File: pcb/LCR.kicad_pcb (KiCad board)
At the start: 2 copper layers, 63.5 x 25.9 mm, 97 parts, among them J1 Conn_01x02_Pin, J2 USB_C_Receptacle, J3 Conn_01x04_Socket, J4 Conn_01x01_Pin, J5 Conn_01x01_Pin, Q1 BSP613, SW1 SW_SPDT, SW2 SW_DIP_x02, SW3 SW_SPST, U1 LM1117DT-3.3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

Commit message: Add/fix missing/wrong vendor(id)
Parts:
- F2: value 150m -> 350m
- F3: value 10mA -> 10m
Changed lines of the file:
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@@
     (property "Sheetfile" "LCR_measurement.kicad_sch")
     (property "Sheetname" "Measurement")
+    (property "Vendor" "DigiKey")
+    (property "VendorId" "MCP6001T-I/OTCT-ND")
     (property "ki_description" "1MHz, Low-Power Op Amp, SOT-23-5")
     (property "ki_keywords" "single opamp")
@@
     (property "Sheetname" "Measurement")
     (property "Vendor" "HTL")
-    (property "VendorId" "100128")
+    (property "VendorId" "103341")
     (property "ki_description" "Unpolarized capacitor")
     (property "ki_keywords" "cap capacitor")
@@
     (property "Sheetfile" "LCR_measurement.kicad_sch")
     (property "Sheetname" "Measurement")
+    (property "Vendor" "HTL")
+    (property "VendorId" "100206")
     (property "ki_description" "Schottky diode")
     (property "ki_keywords" "diode Schottky")
@@
     (property "Sheetfile" "LCR.kicad_sch")
     (property "Sheetname" "")
+    (property "Vendor" "HTL")
+    (property "VendorId" "103444")
     (property "ki_description" "800mA Low-Dropout Linear Regulator, 3.3V fixed output, TO-252")
     (property "ki_keywords" "linear regulator ldo fixed positive")
@@
     (property "Sheetfile" "LCR_measurement.kicad_sch")
     (property "Sheetname" "Measurement")
+    (property "Vendor" "DigiKey")
+    (property "VendorId" "150-MCP3562RT-E/STCT-ND")
     (property "ki_keywords" "MCP3562RT-E/ST")
     (attr smd)
@@
     (property "Sheetfile" "LCR_measurement.kicad_sch")
     (property "Sheetname" "Measurement")
-    (property "Vendor" "HTL")
-    (property "VendorId" "101546")
+    (property "Vendor" "Amazon")
+    (property "VendorId" "B07BDFXFRK")
     (property "ki_description" "Generic connector, single row, 01x04, script generated")
     (property "ki_keywords" "connector")
@@
     (property "Sheetfile" "LCR_measurement.kicad_sch")
     (property "Sheetname" "Measurement")
+    (property "Vendor" "HTL")
+    (property "VendorId" "100206")
     (property "ki_description" "Schottky diode")
     (property "ki_keywords" "diode Schottky")
@@
     (property "Sheetname" "")
     (property "Vendor" "HTL")
-    (property "VendorId" "")
+    (property "VendorId" "101639")
     (property "ki_description" "Fuse")
     (property "ki_keywords" "fuse")
@@
         (effects (font (size 0.6 0.6) (thickness 0.12)))
     )
-    (fp_text value "150m" (at 0 1.82) (layer "F.Fab")
+    (fp_text value "350m" (at 0 1.82) (layer "F.Fab")
         (effects (font (size 1 1) (thickness 0.15)))
     )
@@
     (property "Sheetfile" "LCR_measurement.kicad_sch")
     (property "Sheetname" "Measurement")
+    (property "Vendor" "DigiKey")
+    (property "VendorId" "MCP4921T-E/MSCT-ND")
     (property "ki_description" "12-Bit D/A Converters with SPI Interface")
     (property "ki_keywords" "12-Bit DAC SPI 1ch")
@@
     (property "Sheetname" "Measurement")
     (property "Vendor" "HTL")
-    (property "VendorId" "102944")
+    (property "VendorId" "102967")
     (property "ki_description" "Resistor")
     (property "ki_keywords" "R res resistor")
@@
     (property "Sheetfile" "LCR.kicad_sch")
     (property "Sheetname" "")
-    (property "Vendor" "HTL")
-    (property "VendorId" "101017, 101382")
+    (property "Vendor" "")
+    (property "VendorId" "")
     (property "ki_description" "Mounting Hole with connection")
     (property "ki_keywords" "mounting hole")
@@
     (property "Sheetname" "Measurement")
     (property "Vendor" "HTL")
-    (property "VendorId" "102944")
+    (property "VendorId" "102967")
     (property "ki_description" "Resistor")
     (property "ki_keywords" "R res resistor")
@@
     (property "Sheetfile" "LCR_measurement.kicad_sch")
     (property "Sheetname" "Measurement")
+    (property "Vendor" "HTL")
+    (property "VendorId" "101614")
     (property "ki_description" "Single Pole Single Throw (SPST) switch")
     (property "ki_keywords" "switch lever")
@@
     (property "Sheetfile" "LCR_measurement.kicad_sch")
     (property "Sheetname" "Measurement")
+    (property "Vendor" "HTL")
+    (property "VendorId" "100206")
     (property "ki_description" "Schottky diode")
     (property "ki_keywords" "diode Schottky")
@@
     (property "Sheetfile" "LCR_measurement.kicad_sch")
     (property "Sheetname" "Measurement")
+    (property "Vendor" "HTL")
+    (property "VendorId" "100206")
     (property "ki_description" "Schottky diode")
     (property "ki_keywords" "diode Schottky")
@@
     (property "Sheetfile" "LCR_measurement.kicad_sch")
     (property "Sheetname" "Measurement")
+    (property "Vendor" "HTL")
+    (property "VendorId" "100206")
     (property "ki_description" "Schottky diode")
     (property "ki_keywords" "diode Schottky")
@@
     (property "Sheetfile" "LCR_measurement.kicad_sch")
     (property "Sheetname" "Measurement")
+    (property "Vendor" "HTL")
+    (property "VendorId" "100206")
     (property "ki_description" "Schottky diode")
     (property "ki_keywords" "diode Schottky")
@@
     (property "Sheetfile" "LCR_measurement.kicad_sch")
     (property "Sheetname" "Measurement")
+    (property "Vendor" "HTL")
+    (property "VendorId" "100206")
     (property "ki_description" "Schottky diode")
     (property "ki_keywords" "diode Schottky")
@@
     (property "Sheetfile" "LCR_measurement.kicad_sch")
     (property "Sheetname" "Measurement")
+    (property "Vendor" "HTL")
+    (property "VendorId" "100206")
     (property "ki_description" "Schottky diode")
     (property "ki_keywords" "diode Schottky")
@@
         (effects (font (size 0.6 0.6) (thickness 0.12)) (justify mirror))
     )
-    (fp_text value "10mA" (at 0.635 -1.143 90) (layer "B.Fab")
+    (fp_text value "10m" (at 0.635 -1.143 90) (layer "B.Fab")
         (effects (font (size 1 1) (thickness 0.15)) (justify mirror))
     )
@@
     (property "Sheetfile" "LCR_measurement.kicad_sch")
     (property "Sheetname" "Measurement")
+    (property "Vendor" "HTL")
+    (property "VendorId" "100206")
     (property "ki_description" "Schottky diode")
     (property "ki_keywords" "diode Schottky")
@@
     (property "Sheetfile" "LCR_measurement.kicad_sch")
     (property "Sheetname" "Measurement")
+    (property "Vendor" "HTL")
+    (property "VendorId" "100188")
     (property "ki_description" "Zener diode")
     (property "ki_keywords" "diode")
@@
     (property "Sheetname" "Measurement")
     (property "Vendor" "HTL")
-    (property "VendorId" "102951")
+    (property "VendorId" "102913")
     (property "ki_description" "Resistor")
     (property "ki_keywords" "R res resistor")
@@
     (property "Sheetfile" "LCR_measurement.kicad_sch")
     (property "Sheetname" "Measurement")
+    (property "Vendor" "HTL")
+    (property "VendorId" "100206")
     (property "ki_description" "Schottky diode")
     (property "ki_keywords" "diode Schottky")
@@
     (property "Sheetname" "Measurement")
     (property "Vendor" "HTL")
-    (property "VendorId" "102951")
+    (property "VendorId" "102945")
     (property "ki_description" "Resistor")
     (property "ki_keywords" "R res resistor")

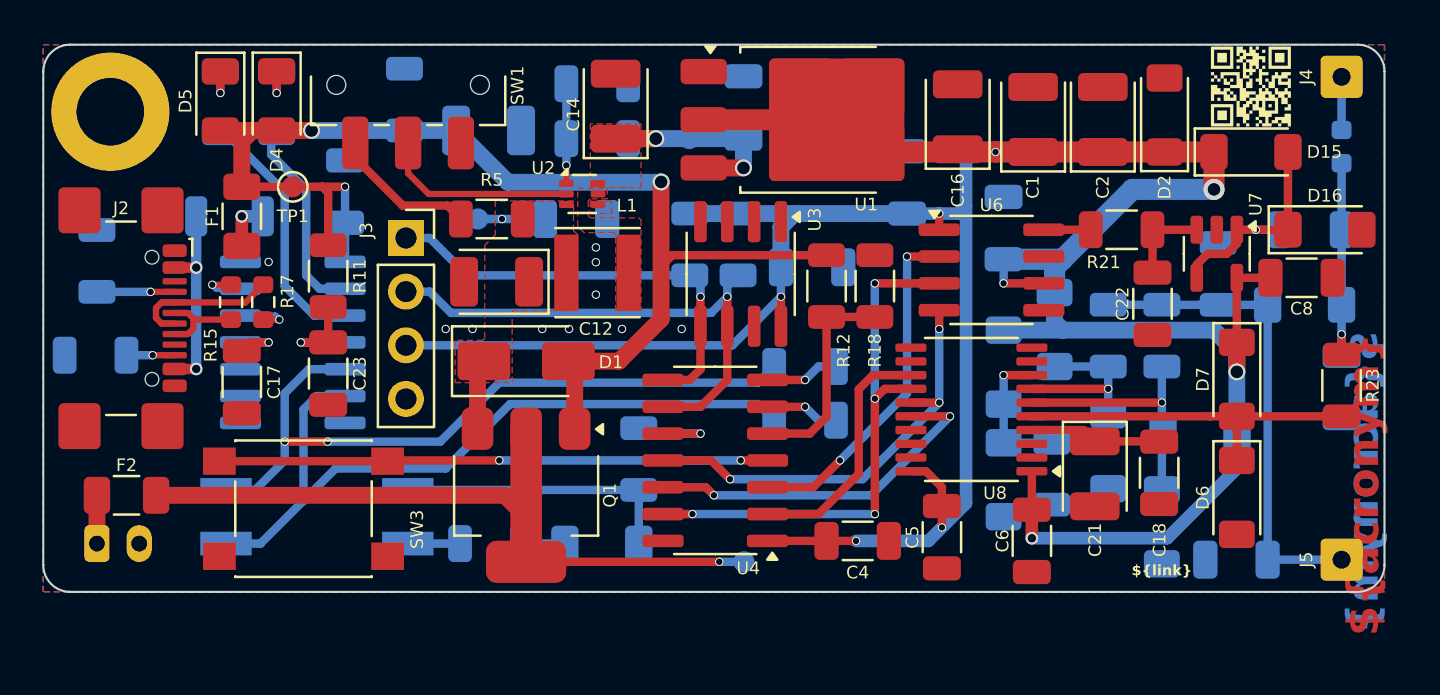
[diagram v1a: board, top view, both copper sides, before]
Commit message: Change MCP2221A to FT230X
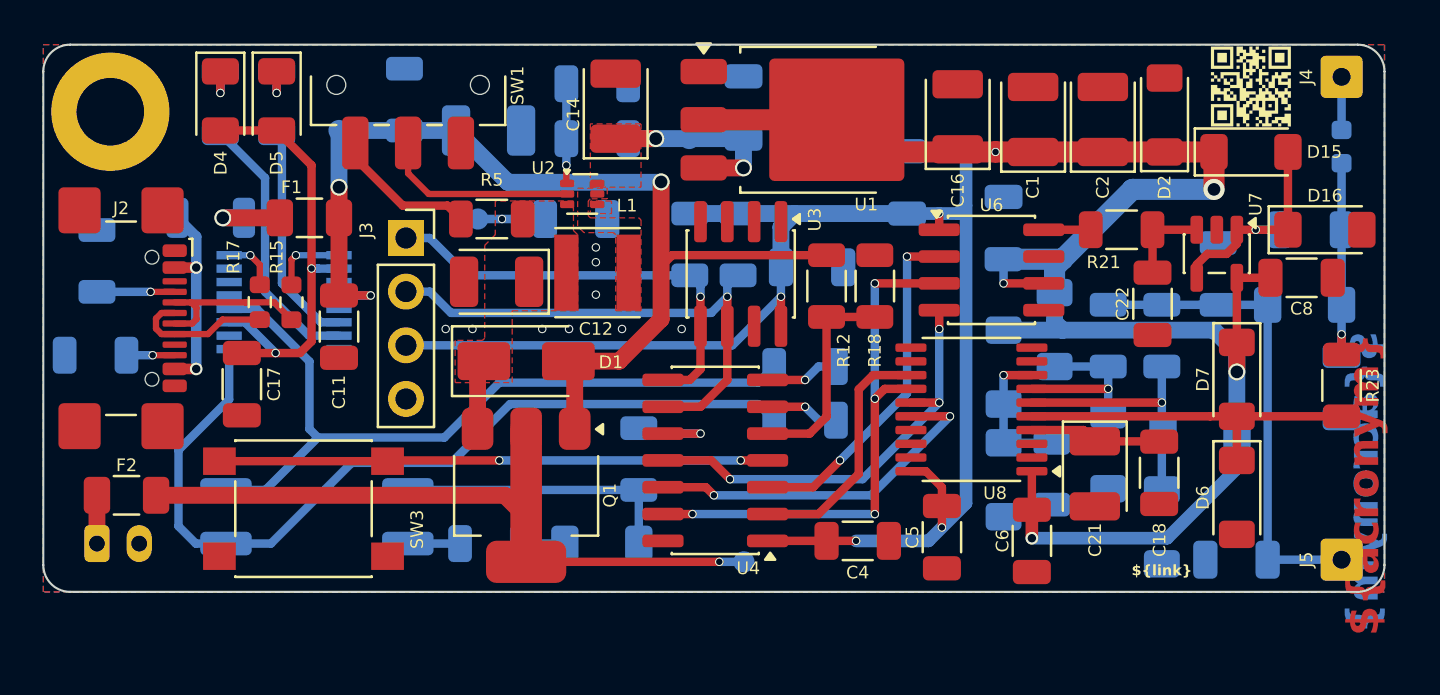
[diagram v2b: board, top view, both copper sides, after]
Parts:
- removed C23: 100n, Capacitor_SMD:C_1206_3216Metric
- removed R11: 1k, Resistor_SMD:R_1206_3216Metric
- C11: moved to F.Cu
- D4: renamed from D5; value Green -> Red
- D5: renamed from D4; value Red -> Green
- TP1: moved to B.Cu
- U5: value MCP2221AxSL -> FT230XS; footprint Package_SO:SOIC-14_3.9x8.7mm_P1.27mm -> Package_SO:SSOP-16_3.9x4.9mm_P0.635mm
- moved C11 6.40 mm to (128.3, 89.5), turned to -90 degrees
- moved TP1 3.45 mm to (128.3, 80.3), turned to 180 degrees
- moved F1 3.20 mm to (126.9, 84.4), turned to 0 degrees
- moved U5 1.95 mm to (125.7, 88.4), turned to 0 degrees
- moved R15 1.36 mm to (124.5, 88.4)
- moved R17 1.34 mm to (126.0, 88.4), turned to 90 degrees
- moved FB1 0.89 mm to (122.2, 84.4)
- moved C17 0.10 mm to (123.7, 92.3)
- renumbered R20 to R19, R19 to R20
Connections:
- C17 pad 1: Net-(U5-VUSB) -> Net-(D4-A)
- D4 pad 2: VBUS -> Net-(D4-A)
- D5 pad 2: VBUS -> Net-(D4-A)
- R13 pad 2: Net-(U5-URx) -> Net-(U5-RXD)
- R14 pad 2: Net-(U5-UTx) -> Net-(U5-TXD)
- R15 pad 2: Net-(U5-D+) -> Net-(U5-USBDP)
- R17 pad 2: Net-(U5-D-) -> Net-(U5-USBDM)
- R19 pad 2: Net-(U5-GP1) -> Net-(U5-CBUS0)
- R20 pad 2: Net-(U5-GP0) -> Net-(U5-CBUS1)
- SW2 pad 1: Net-(U5-UTx) -> Net-(U5-TXD)
- SW2 pad 2: Net-(U5-URx) -> Net-(U5-RXD)
- U5 pad 1: VBUS -> Net-(U5-TXD)
- U5 pad 10: unconnected-(U5-SCL-Pad10) -> Net-(D4-A)
- U5 pad 11: Net-(U5-VUSB) -> Net-(D4-A)
- U5 pad 12: Net-(U5-D-) -> VBUS
- U5 pad 13: Net-(U5-D+) -> GND
- U5 pad 14: GND -> Net-(U5-CBUS1)
- U5 pad 2: Net-(U5-GP0) -> unconnected-(U5-~{RTS}-Pad2)
- U5 pad 3: Net-(U5-GP1) -> Net-(D4-A)
- U5 pad 4: Net-(U5-~{RST}) -> Net-(U5-RXD)
- U5 pad 5: Net-(U5-URx) -> GND
- U5 pad 6: Net-(U5-UTx) -> unconnected-(U5-~{CTS}-Pad6)
- U5 pad 8: unconnected-(U5-GP3-Pad8) -> Net-(U5-USBDP)
- U5 pad 9: unconnected-(U5-SDA-Pad9) -> Net-(U5-USBDM)
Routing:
- net Net-(U5-TXD): track 0.00 -> 41.0 mm
- net Net-(U5-RXD): track 0.00 -> 37.0 mm
- net Net-(U5-UTx): track 35.6 -> 0.00 mm
- net Net-(U5-URx): track 34.5 -> 0.00 mm, vias 2 -> 0
- net Net-(D4-A): track 0.00 -> 21.6 mm, vias 0 -> 2
- net Net-(U5-CBUS0): track 0.00 -> 12.7 mm
- net VBUS: track 62.9 -> 50.2 mm
- net Net-(U5-GP1): track 12.2 -> 0.00 mm
- net Net-(U5-CBUS1): track 0.00 -> 10.7 mm
- net Net-(U5-GP0): track 9.51 -> 0.00 mm
- net Net-(U5-~{RST}): track 5.07 -> 0.00 mm, vias 1 -> 0
- net Net-(U5-USBDM): track 0.00 -> 3.56 mm, vias 0 -> 1
- net Net-(U5-VUSB): track 2.77 -> 0.00 mm, vias 1 -> 0
- net Net-(U5-D-): track 2.68 -> 0.00 mm, vias 1 -> 0
- net Net-(U5-USBDP): track 0.00 -> 2.58 mm, vias 0 -> 1
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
